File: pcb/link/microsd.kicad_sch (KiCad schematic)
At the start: 29 parts, among them J2 MEM2061-01-188-00-A, J6 FFC2B35-10-T, U11 TPS2021D, U3 TS3DV416DGGR

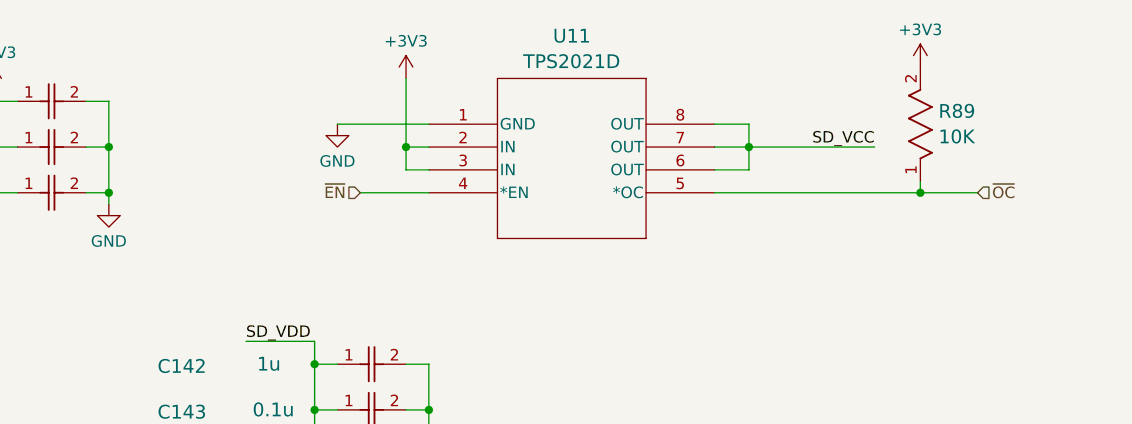
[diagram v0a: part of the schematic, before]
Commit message: add pullup to sdcard EN (closes #106)
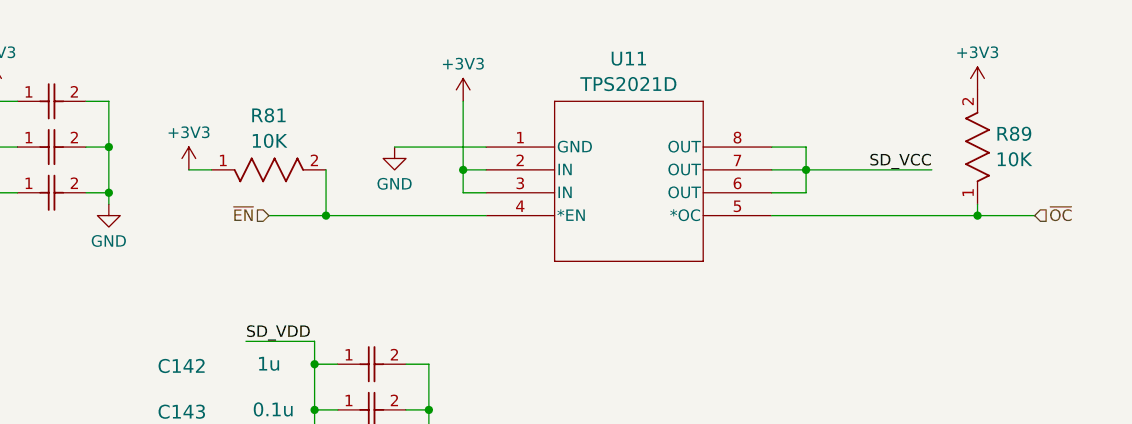
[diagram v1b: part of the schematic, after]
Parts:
- added R81: 10K, OroLink:STA_RMCF0402_STP, symbol OroLink:RMCF0402FT10K0
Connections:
- net +3V3: now also R81.1
- net ~{EN}: now also R81.2
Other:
- moved on the sheet: R89, U11

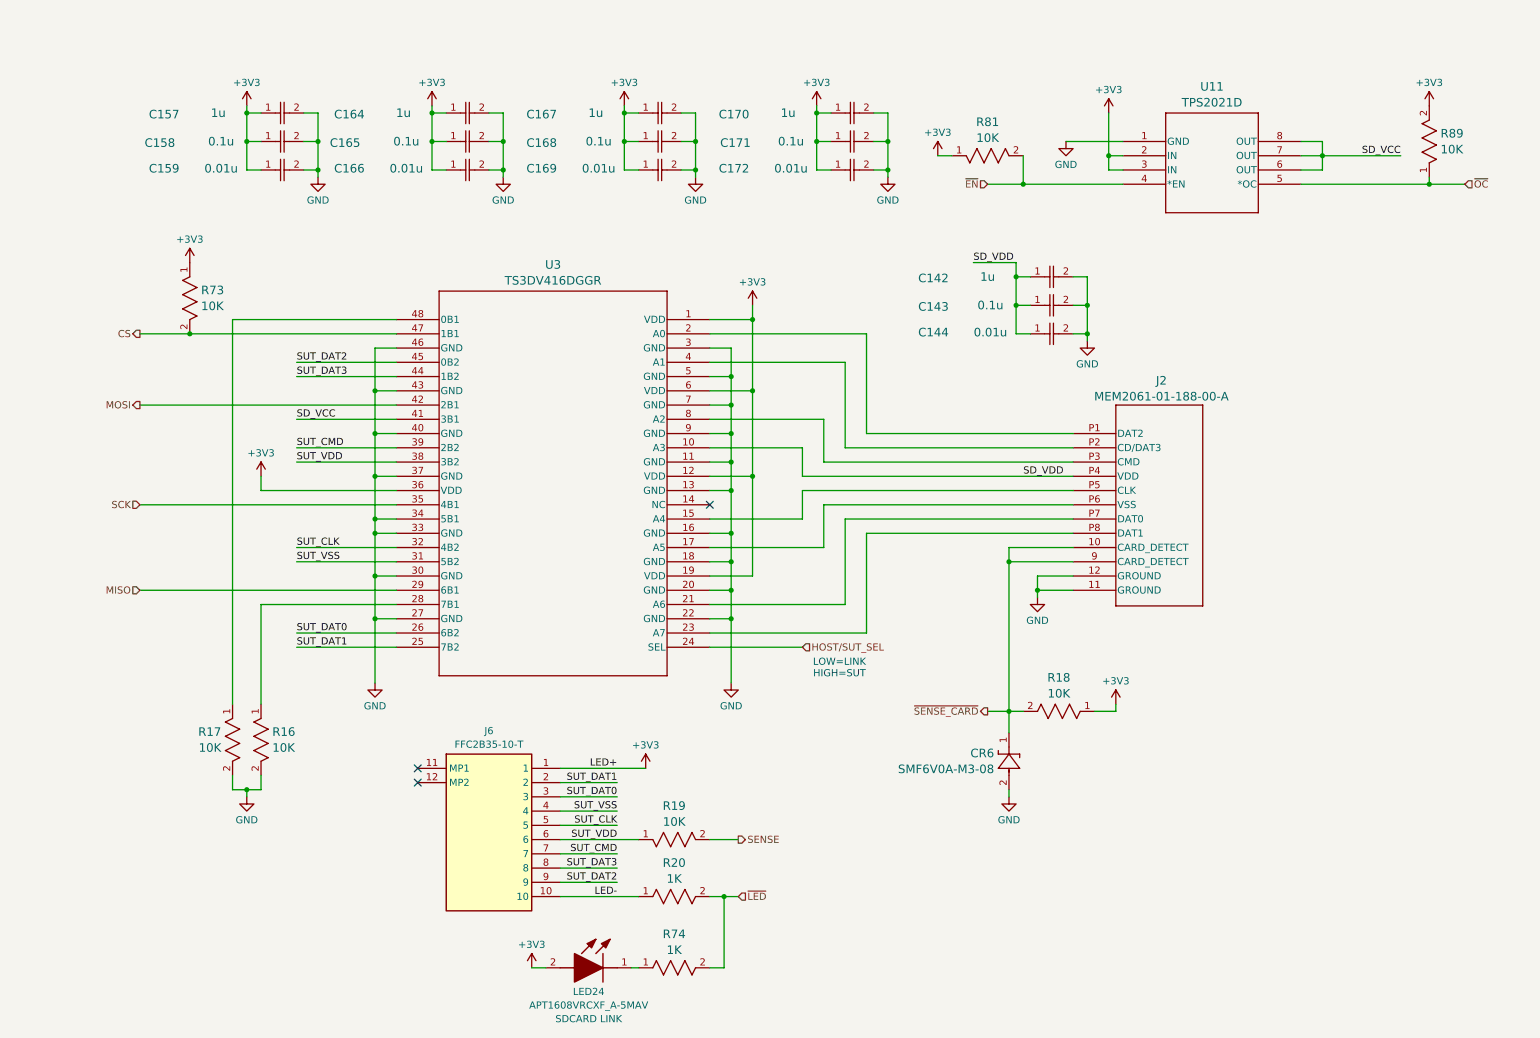
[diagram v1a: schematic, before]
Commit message: add filtering caps on TPS gates (closes #107)
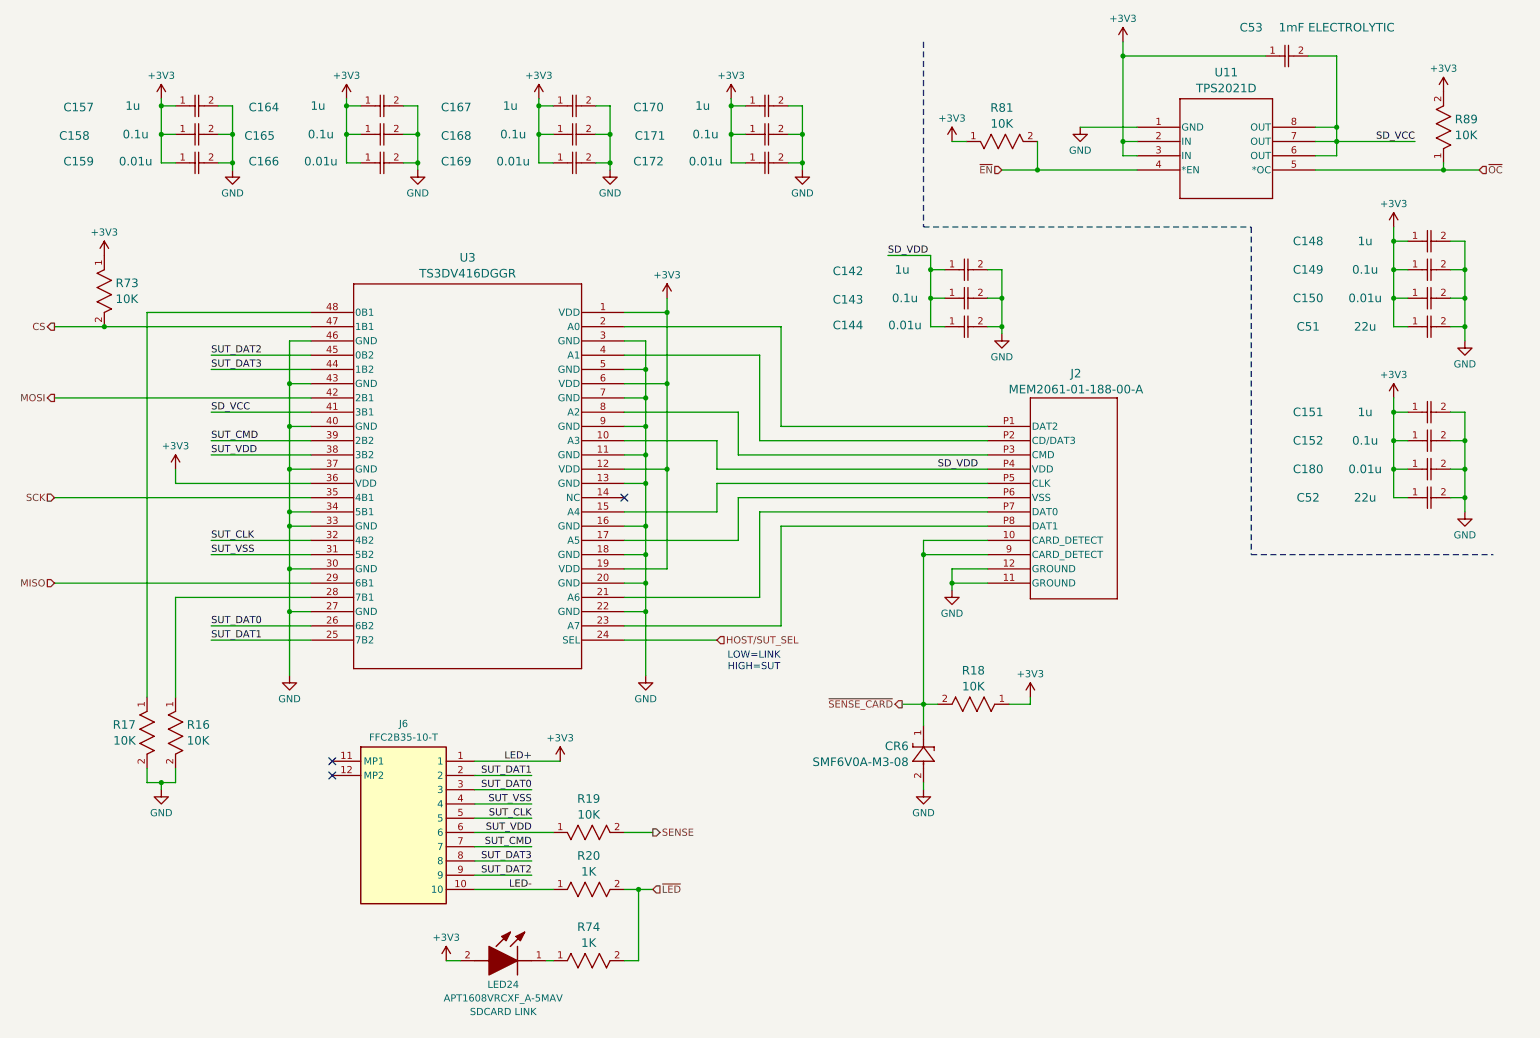
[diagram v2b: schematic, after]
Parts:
- added C148, C151: 1u, OroLink:cap_UMK105 CG080CV-F_TAY, symbol OroLink:JMK105BJ105KVHF
- added C149, C152: 0.1u, OroLink:CAP_MSAS1L-3_TAY, symbol OroLink:MSAST1L3YB5104KFNA01
- added C150, C180: 0.01u, OroLink:CAP_0402_N_WAL, symbol OroLink:0402B103J160CT
- added C51, C52: 22u, OroLink:CAP_CM05_K_KAV, symbol OroLink:CM05X5R226M06AH080
- added C53: 1mF ELECTROLYTIC, OroLink:CAP_99614E3_VIS, symbol OroLink:MAL215099614E3
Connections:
- net +3V3: now also C148.1, C149.1, C150.1, C151.1, C152.1, C180.1, C51.1, C52.1, C53.1
- net GND: now also C148.2, C149.2, C150.2, C151.2, C152.2, C180.2, C51.2, C52.2
- net SD_VCC: now also C53.2
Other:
- moved on the sheet: C142, C143, C144, C157, C158, C159, C164, C165, C166, C167, C168, C169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
